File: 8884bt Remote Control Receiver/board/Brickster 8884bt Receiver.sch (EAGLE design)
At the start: 22 parts, among them J1 AVR_SPI_PRG_6NS, J2 CON_PF, J3 CON_PF, J4 CON_PF, U1 IC_ATTINY_X4A, U2 IC_TB6612FNG, U3 IC_RT9164A, U4 BLUETOOTH-RN41"

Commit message: Update receiver to revision 1a
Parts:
- removed B1, B2: B_CDBHM240L-HF, brickster:B_CDBHM240L-HF
- removed C4: 0.1uF, brickster:C
- removed D2: D, brickster:D
- added Q1, Q2: IC_FET_BRIDGESO8, brickster:IC_FET_BRIDGESO8
- B3, B4: value B_MDB8S -> B_CDBHM240L-HF; device brickster:B_MDB8S -> brickster:B_CDBHM240L-HF
- C1, C3: device brickster:C -> brickster:C0805
- R1: device brickster:R -> brickster:R0805
- R2: value 1k -> 3.3k; device brickster:R -> brickster:R0805
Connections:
- removed net N$1: D2.P$1, J1.2
- new net PF_GND: J2.P$4, Q1.N1D/P1D, Q1.N2G, Q1.P2G
- net 3.3V: now also J1.2, U3.P$1; no longer C4.1
- net A01: now also B3.AC2; no longer B3.AC1
- net A02: now also B3.AC1; no longer B3.AC2
- net AIN1: now also U1.(PCINT1/AIN0/ADC1)PA1; no longer U1.(PCINT10/INT0/OC0A/CKOUT)PB2
- net AIN2: now also U1.(PCINT2/AIN1/ADC2)PA2; no longer U1.(PCINT9/XTAL2)PB1
- net ATRX/BTTX: now also U1.(PCINT8/XTAL1/CLKI)PB0; no longer U1.(PCINT2/AIN1/ADC2)PA2
- net ATTX/BTRX: now also U1.(PCINT9/XTAL2)PB1; no longer U1.(PCINT7/ICP/OC0B/ADC7)PA7
- net B01: now also B4.AC2; no longer B4.AC1
- net B02: now also B4.AC1; no longer B4.AC2
- net BIN1: now also U1.(PCINT0/AREF/ADC0)PA0; no longer U1.(PCINT3/T0/ADC3)PA3
- net BIN2: now also U1.(PCINT10/INT0/OC0A/CKOUT)PB2; no longer U1.(PCINT1/AIN0/ADC1)PA1
- net BLUE: now also D1G$1.P$2, D1G$2.P$1; no longer D1G$1.P$1, D1G$2.P$2
- net GND: now also Q1.N1S/N2S, Q2.N1S/N2S; no longer B1.-, B1.AC2, B2.-, C4.2, J2.P$4
- net N$16: now also D1G$1.P$1, D1G$2.P$2; no longer D1G$1.P$2, D1G$2.P$1
- net PF_9V: now also Q1.N1G, Q1.N2D/P2D, Q1.P1G; no longer B1.AC1
- net PF_C1: now also Q2.N1G, Q2.N2D/P2D, Q2.P1G; no longer B2.AC2
- net PF_C2: now also Q2.N1D/P1D, Q2.N2G, Q2.P2G; no longer B2.AC1
- net PWMA: now also U1.(PCINT3/T0/ADC3)PA3; no longer U1.(PCINT8/XTAL1/CLKI)PB0
- net PWMB: now also U1.(PCINT7/ICP/OC0B/ADC7)PA7; no longer U1.(PCINT0/AREF/ADC0)PA0
- net VIN: now also Q1.P1S/P2S, Q2.P1S/P2S; no longer B1.+, B2.+, D2.P$2
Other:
- note added: "1a"
- note removed: "1"
- moved on the sheet: B3, B4, C1, C2, C3, C5, D1G$1, D1G$2, J1, J2, J3, J4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

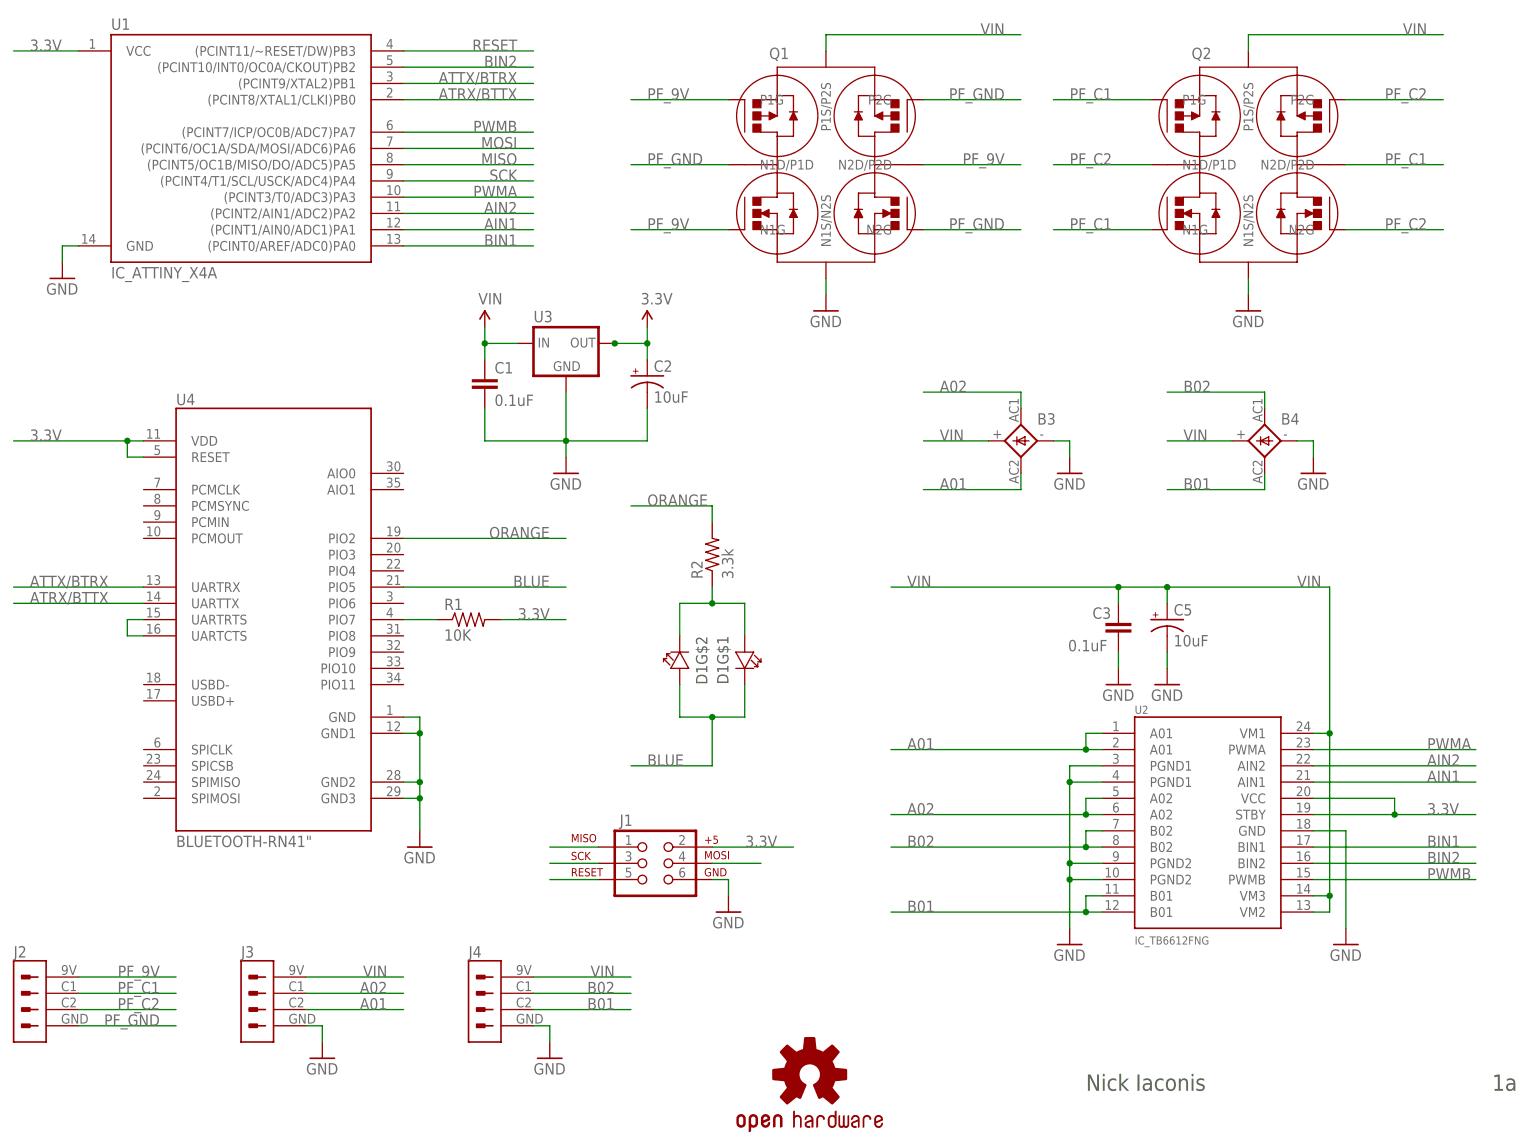
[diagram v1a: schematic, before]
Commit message: Add drv8833 to library and schematic
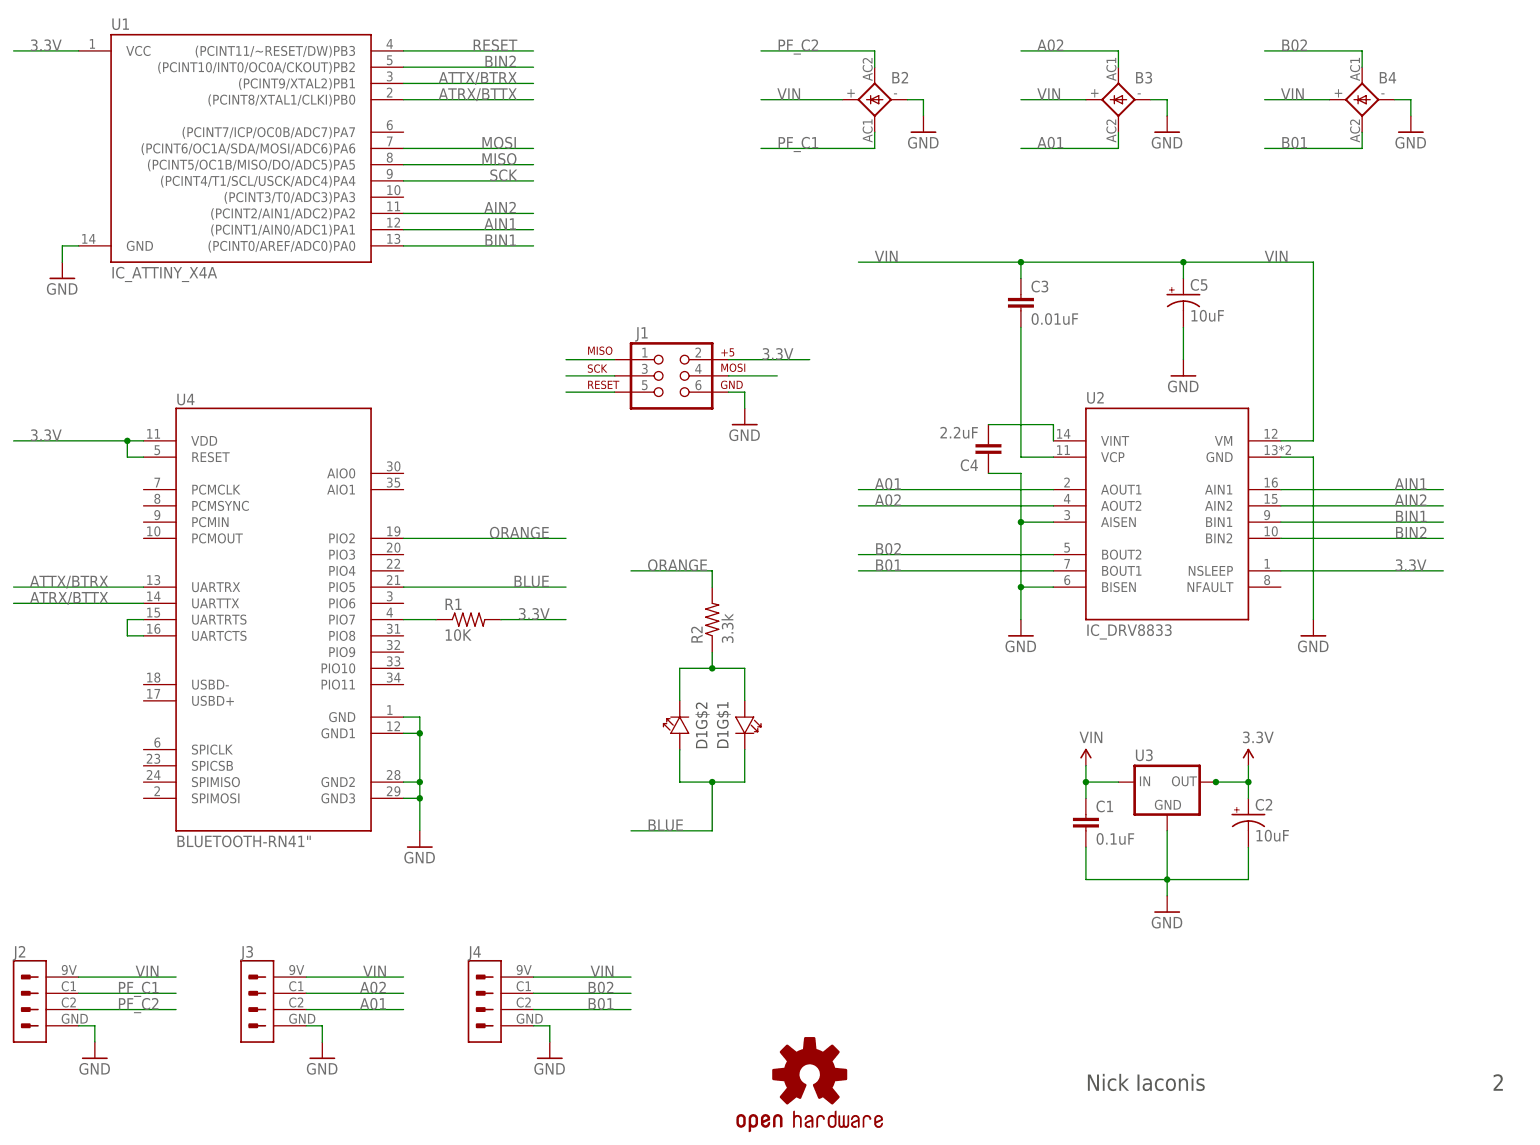
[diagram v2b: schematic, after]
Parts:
- removed Q1, Q2: IC_FET_BRIDGESO8, brickster:IC_FET_BRIDGESO8
- added B2: B_MDB8S, brickster:B_MDB8S
- added C4: 2.2uF, brickster:C0805
- C3: value 0.1uF -> 0.01uF
- U2: value IC_TB6612FNG -> IC_DRV8833; device brickster:IC_TB6612FNG -> brickster:IC_DRV8833
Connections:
- removed net PF_9V: J2.P$1, Q1.N1G, Q1.N2D/P2D, Q1.P1G
- removed net PF_GND: J2.P$4, Q1.N1D/P1D, Q1.N2G, Q1.P2G
- removed net PWMA: U1.(PCINT3/T0/ADC3)PA3, U2.PWMA
- removed net PWMB: U1.(PCINT7/ICP/OC0B/ADC7)PA7, U2.PWMB
- new net N$1: C3.2, U2.VCP
- new net N$2: C4.2, U2.VINT
- net 3.3V: now also U2.NSLEEP; no longer U2.STBY, U2.VCC
- net A01: now also U2.AOUT1; no longer U2.A01@1, U2.A01@2
- net A02: now also U2.AOUT2; no longer U2.A02@5, U2.A02@6
- net B01: now also U2.BOUT1; no longer U2.B01@11, U2.B01@12
- net B02: now also U2.BOUT2; no longer U2.B02@7, U2.B02@8
- net GND: now also B2.-, C4.1, J2.P$4, U2.AISEN, U2.BISEN; no longer C3.2, Q1.N1S/N2S, Q2.N1S/N2S, U2.PGND1@3, U2.PGND1@4, U2.PGND2@10, U2.PGND2@9
- net PF_C1: now also B2.AC1; no longer Q2.N1G, Q2.N2D/P2D, Q2.P1G
- net PF_C2: now also B2.AC2; no longer Q2.N1D/P1D, Q2.N2G, Q2.P2G
- net VIN: now also B2.+, J2.P$1, U2.VM; no longer Q1.P1S/P2S, Q2.P1S/P2S, U2.VM1, U2.VM2, U2.VM3
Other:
- note added: "2"
- note removed: "1a"
- moved on the sheet: B3, B4, C1, C2, C3, C5, D1G$1, D1G$2, J1, R2, U3

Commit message: Route rev. 2 board
Need to change OSH logo to t/b-stop
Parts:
- removed R1: 10K, brickster:R0805
- B2: value B_MDB8S -> B_CDBHM240L-HF; device brickster:B_MDB8S -> brickster:B_CDBHM240L-HF
- D1: value Blue/Orange -> LED0805; device brickster:LED_LTST_C195TBKFKT -> brickster:LED0805
- U4: value BLUETOOTH-RN41" -> HC-06; device SparkFun-RF:BLUETOOTH-RN41" -> brickster:HC-06
- renumbered LOGO1 to LOGO2
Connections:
- removed net BLUE: D1G$1.P$2, D1G$2.P$1, U4.PIO5
- removed net N$15: R1.1, U4.PIO7
- removed net N$16: D1G$1.P$1, D1G$2.P$2, R2.1
- removed net ORANGE: R2.2, U4.PIO2
- new net BTRST: U1.(PCINT3/T0/ADC3)PA3, U4.RESET
- new net KEY: U1.(PCINT2/AIN1/ADC2)PA2, U4.PIO3
- new net LED: R2.1, U4.PIO1
- new net N$4: D1.P$1, R2.2
- net 3.3V: no longer R1.2, U4.RESET
- net A01: now also B3.AC1; no longer B3.AC2
- net A02: now also B3.AC2; no longer B3.AC1
- net AIN1: now also U1.(PCINT8/XTAL1/CLKI)PB0; no longer U1.(PCINT1/AIN0/ADC1)PA1
- net AIN2: now also U1.(PCINT9/XTAL2)PB1; no longer U1.(PCINT2/AIN1/ADC2)PA2
- net ATRX/BTTX: now also U1.(PCINT0/AREF/ADC0)PA0; no longer U1.(PCINT8/XTAL1/CLKI)PB0
- net ATTX/BTRX: now also U1.(PCINT1/AIN0/ADC1)PA1; no longer U1.(PCINT9/XTAL2)PB1
- net BIN1: now also U1.(PCINT7/ICP/OC0B/ADC7)PA7; no longer U1.(PCINT0/AREF/ADC0)PA0
- net GND: now also D1.P$2; no longer U4.GND3
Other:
- moved on the sheet: D1, R2

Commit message: Route rev. 2 board
Use SMD pads for Power Functions connections
(threading PF wire through tiny vias is too difficult)
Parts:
- removed LOGO2: OSHW-LOGOM, SparkFun-Aesthetics:OSHW-LOGOM
- J2, J3, J4: value CON_PF -> CON_PF_SMD; device brickster:CON_PF -> brickster:CON_PF_SMD
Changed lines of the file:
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@@
 <part name="SUPPLY6" library="SparkFun-Aesthetics" deviceset="VIN" device=""/>
 <part name="FRAME1" library="SparkFun-Aesthetics" deviceset="FRAME_LETTER_BLANK" device=""/>
-<part name="LOGO2" library="SparkFun-Aesthetics" deviceset="OSHW-LOGO" device="M"/>
 <part name="C1" library="brickster" deviceset="C" device="0805" value="0.1uF"/>
 <part name="C2" library="brickster" deviceset="C_POL" device="" value="10uF"/>
@@
 <part name="GND7" library="SparkFun" deviceset="GND" device=""/>
 <part name="GND14" library="SparkFun" deviceset="GND" device=""/>
-<part name="J2" library="brickster" deviceset="CON_PF" device=""/>
-<part name="J3" library="brickster" deviceset="CON_PF" device=""/>
-<part name="J4" library="brickster" deviceset="CON_PF" device=""/>
+<part name="J2" library="brickster" deviceset="CON_PF" device="_SMD"/>
+<part name="J3" library="brickster" deviceset="CON_PF" device="_SMD"/>
+<part name="J4" library="brickster" deviceset="CON_PF" device="_SMD"/>
 <part name="GND6" library="SparkFun" deviceset="GND" device=""/>
 <part name="U2" library="brickster" deviceset="IC_DRV8833" device=""/>
@@
 <instance part="FRAME1" gate="G$1" x="101.6" y="20.32"/>
 <instance part="FRAME1" gate="G$2" x="248.92" y="20.32"/>
-<instance part="LOGO2" gate="G$1" x="236.22" y="30.48"/>
 <instance part="C1" gate="G$1" x="279.4" y="68.58"/>
 <instance part="C2" gate="G$1" x="304.8" y="71.12"/>
